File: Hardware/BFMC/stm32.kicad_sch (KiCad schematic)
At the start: 6 parts, among them J3 INIT_BLDC, U1 NUCLEO-F401RE

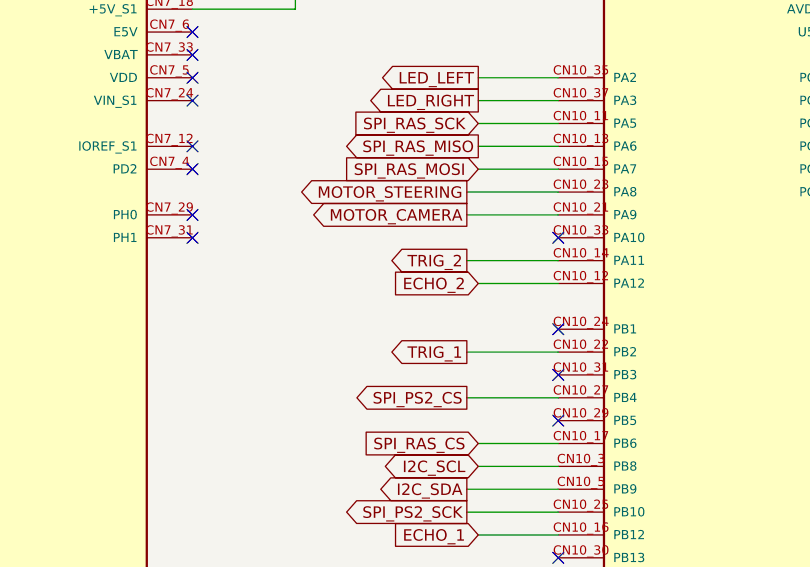
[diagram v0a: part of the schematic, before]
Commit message: update temporary file in stm32
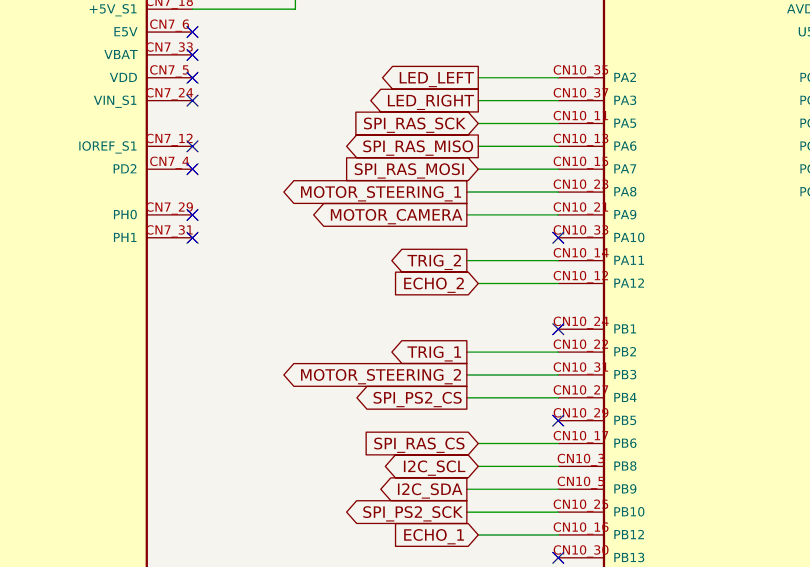
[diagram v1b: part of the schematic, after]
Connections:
- net MOTOR_STEERING_2: now reaches U1.CN10_31 (PB3)
- net MOTOR_STEERING renamed MOTOR_STEERING_1
- no-connect marks 34 -> 33
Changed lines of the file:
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@@
   (no_connect (at 138.43 80.01))
   (no_connect (at 97.79 59.69))
-  (no_connect (at 138.43 95.25))
   (no_connect (at 173.99 125.73))
   (no_connect (at 57.15 123.19))
@@
     (stroke (width 0) (type default))
   )
+  (wire (pts (xy 128.27 95.25) (xy 138.43 95.25))
+    (stroke (width 0) (type default))
+  )
   (wire (pts (xy 46.99 80.01) (xy 57.15 80.01))
     (stroke (width 0) (type default))
@@
     )
   )
+  (global_label "MOTOR_STEERING_2" (shape output) (at 128.27 95.25 180) (fields_autoplaced)
+    (effects (font (size 1.27 1.27)) (justify right))
+    (property "Intersheetrefs" "${INTERSHEET_REFS}" (at 106.8397 95.25 0)
+      (effects (font (size 1.27 1.27)) (justify right) hide)
+    )
+  )
   (global_label "SPI_PS2_CS" (shape output) (at 128.27 97.79 180) (fields_autoplaced)
     (effects (font (size 1.27 1.27)) (justify right))
@@
     )
   )
-  (global_label "MOTOR_STEERING" (shape output) (at 128.27 74.93 180) (fields_autoplaced)
-    (effects (font (size 1.27 1.27)) (justify right))
-    (property "Intersheetrefs" "${INTERSHEET_REFS}" (at 109.0168 74.93 0)
-      (effects (font (size 1.27 1.27)) (justify right) hide)
-    )
+  (global_label "MOTOR_STEERING_1" (shape output) (at 128.27 74.93 180) (fields_autoplaced)
+    (effects (font (size 1.27 1.27)) (justify right))
+    (property "Intersheetrefs" "${INTERSHEET_REFS}" (at 106.8397 74.93 0)
+      (effects (font (size 1.27 1.27)) (justify right) hide)
+    )
